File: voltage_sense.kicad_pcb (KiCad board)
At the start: 6 copper layers, 48 x 28 mm, 53 parts, among them IC1 DAC101C081CIMK_NOPB, J1 Conn_Coaxial, J2 Conn_01x04, J4 HDMI_A, J5 Conn_Coaxial, U1 OPA188xxDBV, U2 ADA4000-1, U3 OPA188xxDBV, U4 MCP4017T-103E_LT, U5 OPA1641, U6 24AA025UID, U9 LP2981A-33DBVT

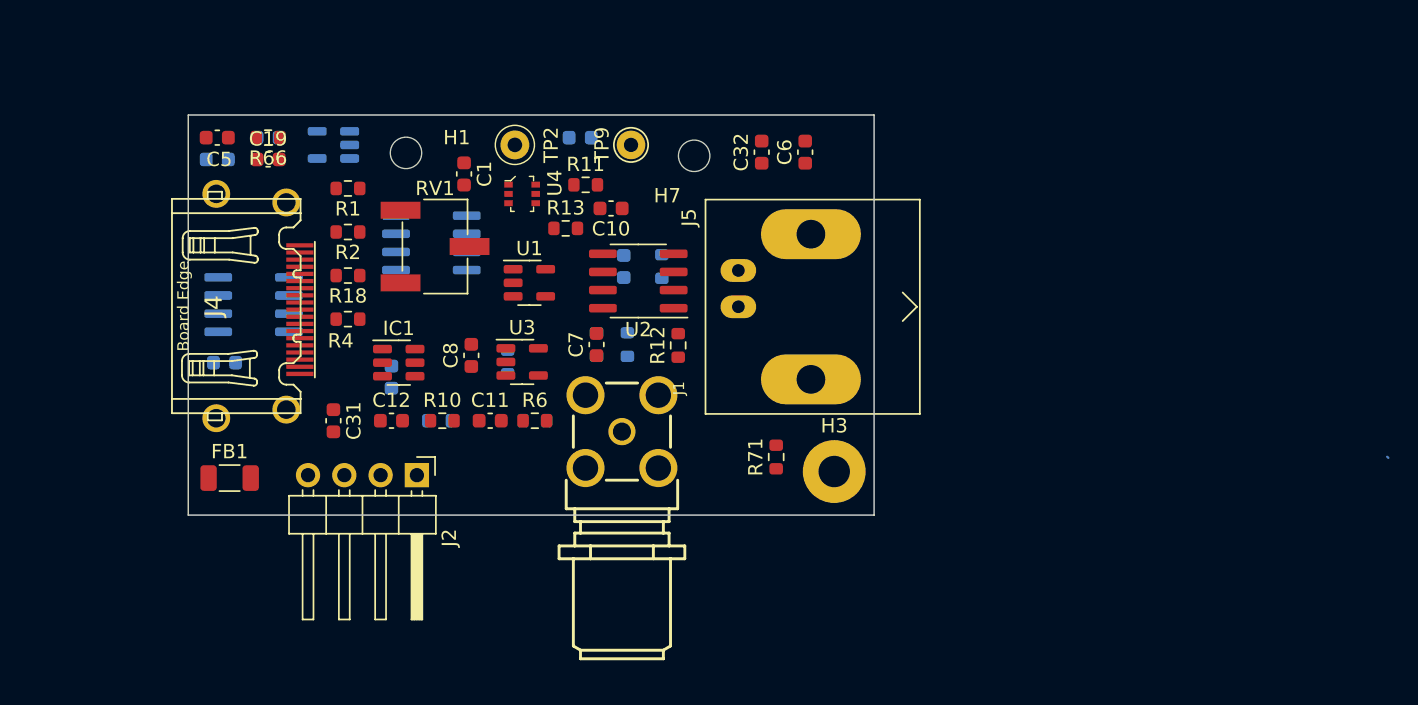
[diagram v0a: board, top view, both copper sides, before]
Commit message: found LCSC alternatives for some parts
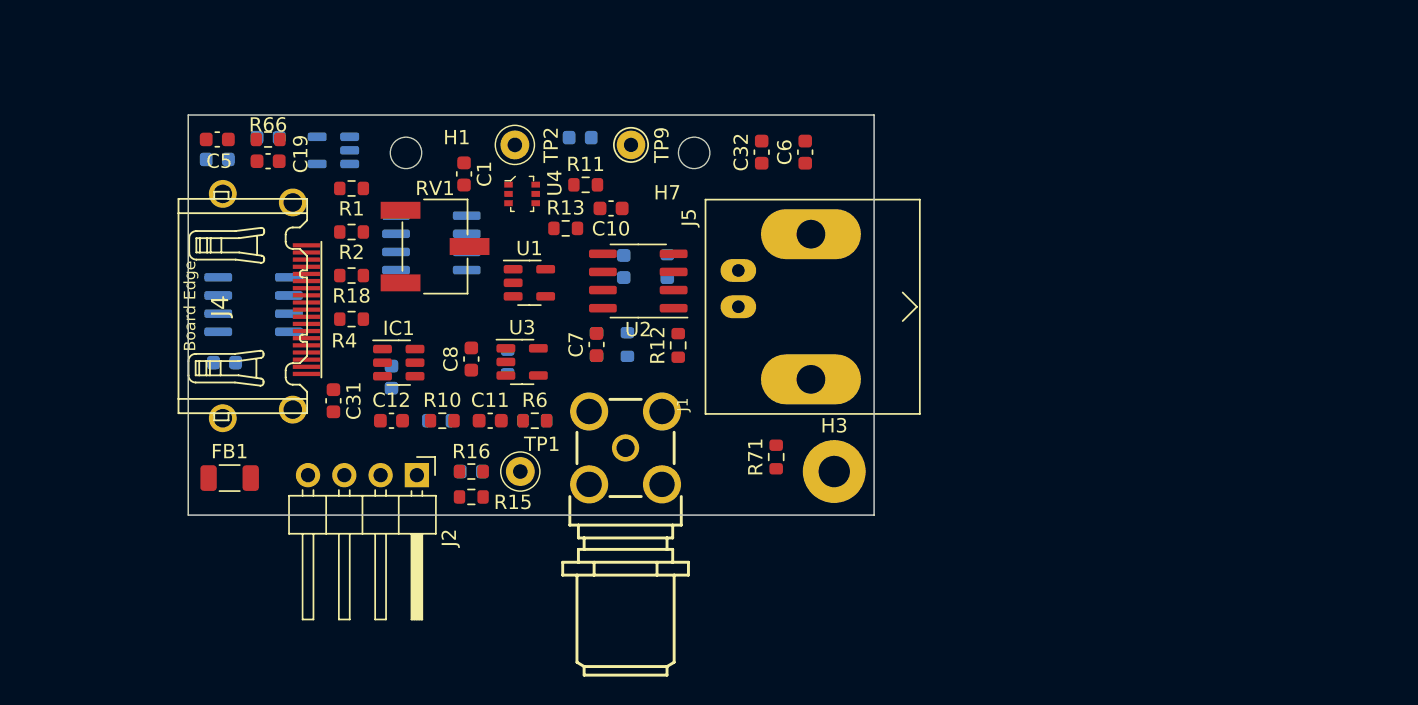
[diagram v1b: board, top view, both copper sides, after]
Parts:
- added C13: DNI, Capacitor_SMD:C_0603_1608Metric, B.Cu at (19.8, -3.05)
- added R15: 30k, Resistor_SMD:R_0603_1608Metric, F.Cu at (19.8, -1.27)
- added R16: 3k, Resistor_SMD:R_0603_1608Metric, F.Cu at (19.8, -3.05)
- added TP1: RCT-0C, digikey-footprints:Test_Point_D1.02mm, F.Cu at (23.2, -3.05)
- R14: value DNI -> 33
- moved C31 1.40 mm to (10.2, -8.00)
- moved J1 1.17 mm to (30.6, -4.70)
- moved J4 0.46 mm to (4.32, -14.6)
- moved R8 0.38 mm to (33.5, -17.4)
- moved U9 0.38 mm to (10.2, -25.5)
- moved C8 0.25 mm to (19.8, -10.9)
- moved R1 0.25 mm to (11.4, -22.9)
- moved R18 0.25 mm to (11.4, -16.8)
- moved R2 0.25 mm to (11.4, -19.8)
- moved R4 0.25 mm to (11.4, -13.7)
- moved H7 0.20 mm to (35.4, -25.4)
- moved C19 0.13 mm to (5.59, -24.8), turned to 180 degrees
- moved C5 0.13 mm to (2.03, -26.3)
- moved R66 0.13 mm to (5.59, -26.3)
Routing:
- net (no net): track 43.0 -> 0.00 mm
- net Net-(FB1-Pad1): track 40.6 -> 0.00 mm
- net /vsense/CMD: track 38.1 -> 0.00 mm
- net GND: track 34.4 -> 0.00 mm
- net /vsense/SMA_OUT: track 16.4 -> 0.00 mm
- net /vsense/AMP_OUT: track 15.4 -> 0.00 mm
- net +5V: track 14.3 -> 0.00 mm
- net /vsense/SDA: track 9.48 -> 0.00 mm
- net +3V3: track 4.87 -> 0.00 mm

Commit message: first draft of production files
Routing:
- net +3V3: track 0.00 -> 46.2 mm, vias 0 -> 3
- net GND: track 0.00 -> 39.3 mm, vias 0 -> 28
- net Net-(C12-Pad1): track 0.00 -> 31.9 mm, vias 0 -> 2
- net /vsense/SCL: track 0.00 -> 31.6 mm
- net Net-(C12-Pad2): track 0.00 -> 31.5 mm, vias 0 -> 1
- net Net-(FB1-Pad1): track 0.00 -> 29.5 mm
- net /vsense/SDA: track 0.00 -> 29.1 mm
- net Net-(C7-Pad2): track 0.00 -> 28.6 mm, vias 0 -> 2
- net Net-(R12-Pad1): track 0.00 -> 23.3 mm, vias 0 -> 1
- net /vsense/CC: track 0.00 -> 18.0 mm
- net Net-(C7-Pad1): track 0.00 -> 17.9 mm, vias 0 -> 1
- net Net-(C8-Pad2): track 0.00 -> 17.0 mm, vias 0 -> 1
- net /vsense/CMD: track 0.00 -> 15.4 mm
- net Net-(C1-Pad2): track 0.00 -> 14.9 mm
- net Net-(IC1-Pad1): track 0.00 -> 12.9 mm
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
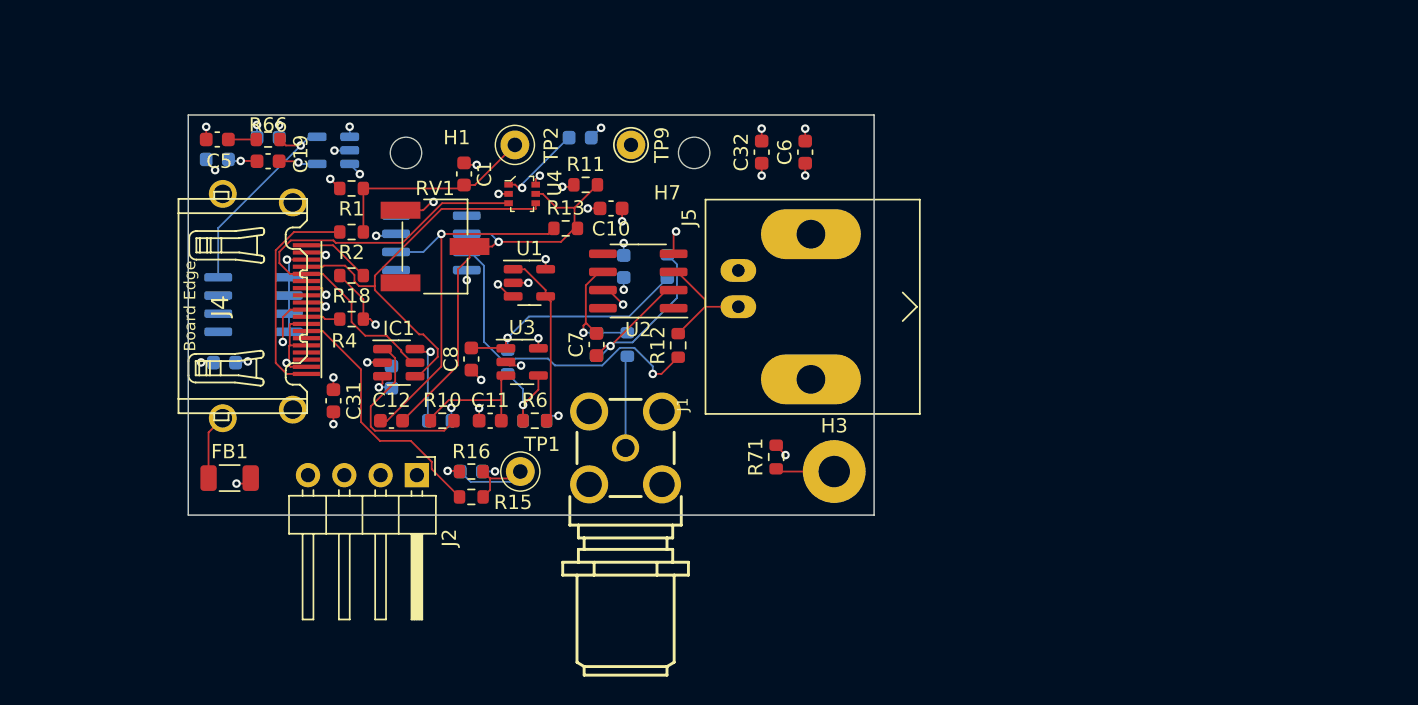
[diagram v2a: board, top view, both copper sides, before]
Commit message: moved SMA to same size as HDMI
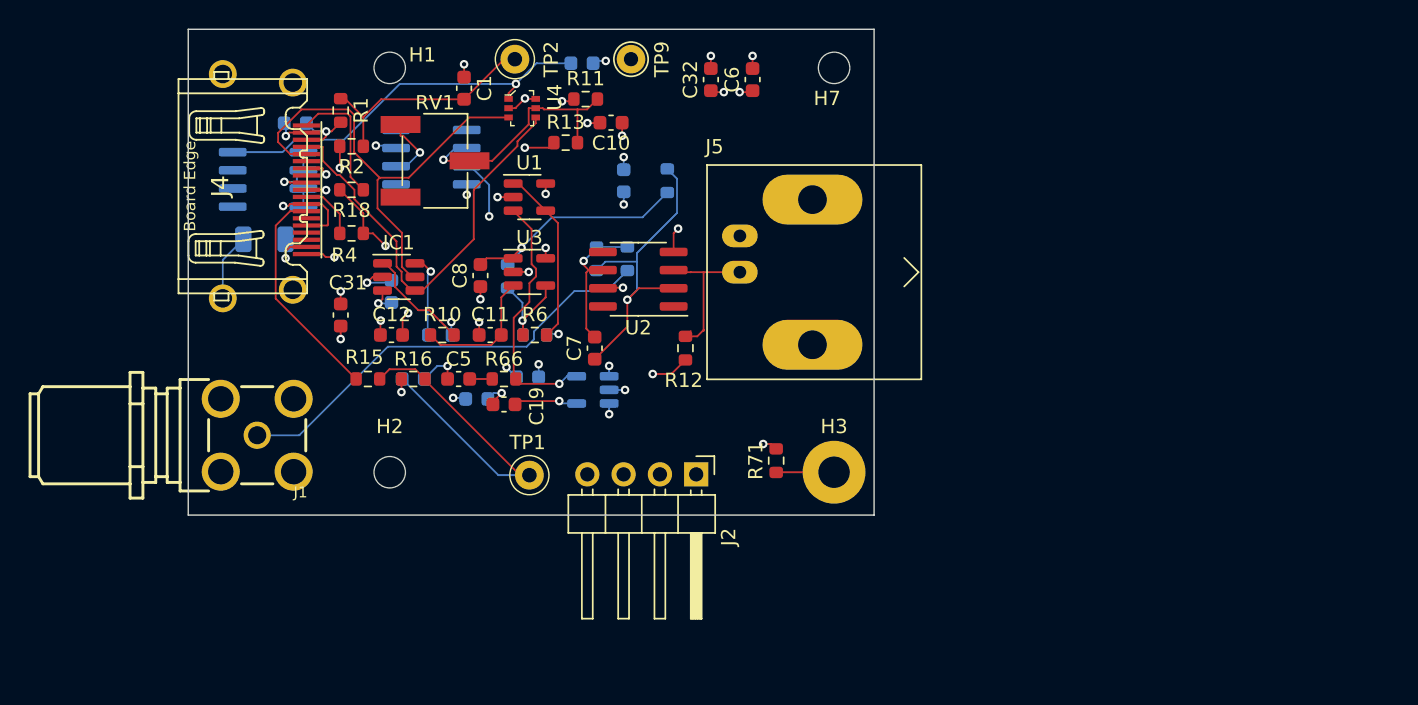
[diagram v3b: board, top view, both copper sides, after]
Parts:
- added H2: DNI, MountingHole:MountingHole_2.2mm_M2, F.Cu at (14.1, -3.00)
- C19: value 0.01u -> DNI
- FB1: moved to B.Cu
- moved J1 25.8 mm to (4.83, -5.59), turned to 180 degrees
- moved C2 24.7 mm to (20.2, -8.13)
- moved U9 24.7 mm to (28.3, -8.76)
- moved C4 24.7 mm to (23.7, -9.65)
- moved C5 23.8 mm to (18.9, -9.53)
- moved C19 23.7 mm to (22.1, -7.75)
- moved R66 23.5 mm to (22.1, -9.53)
- moved J2 19.5 mm to (35.5, -2.85)
- moved C39 17.5 mm to (7.49, -27.4), turned to 180 degrees
- moved FB1 16.9 mm to (5.33, -19.3)
- moved H7 11.5 mm to (45.2, -31.3)
- moved R15 11.0 mm to (12.6, -9.53)
- moved U6 8.82 mm to (5.59, -23.5)
- moved J4 8.39 mm to (4.32, -23.0)
- moved C13 7.65 mm to (15.7, -9.53)
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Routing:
- net /vsense/SMA_OUT: track 6.47 -> 31.0 mm
- net +3V3: track 46.2 -> 67.5 mm, vias 3 -> 2
- net Net-(C13-Pad2): track 9.30 -> 25.6 mm
- net GND: track 39.3 -> 44.7 mm, vias 28 -> 24
- net /vsense/CMD: track 15.4 -> 9.96 mm, vias 0 -> 2
- net Net-(IC1-Pad1): track 12.9 -> 7.65 mm
- net Net-(C7-Pad1): track 17.9 -> 22.6 mm
- net /vsense/AMP_OUT: track 4.86 -> 9.01 mm
- net Net-(C12-Pad1): track 31.9 -> 28.3 mm, vias 2 -> 3
- net +15V: track 11.0 -> 8.42 mm
- net /vsense/CC: track 18.0 -> 15.6 mm
- net Net-(J5-Pad1): track 8.49 -> 10.8 mm
- net /vsense/CAL_ADC: track 2.41 -> 4.19 mm
- net Net-(C19-Pad1): track 2.74 -> 4.48 mm
- net /vsense/SCL: track 31.6 -> 33.3 mm
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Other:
- board size 48 x 28 mm -> 48 x 34 mm

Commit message: files sent to JLCPCB; Order Y10-3276043A, SMT02305291257986-3276043A
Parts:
- C13, C2, C3, C39, C4, C47, C9, FB1, R14, R3, R5, R7, R8, R9, U9: moved to F.Cu
- moved C10 26.9 mm to (7.75, -11.8), turned to 90 degrees
- moved C12 23.7 mm to (37.5, -8.00), turned to 180 degrees
- moved R13 23.1 mm to (40.8, -8.00)
- moved R14 22.6 mm to (11.2, -6.60), turned to 0 degrees
- moved U5 22.3 mm to (31.4, -8.00)
- moved R11 16.4 mm to (44.1, -26.7), turned to 90 degrees
- moved U4 16.3 mm to (39.6, -26.8), turned to 0 degrees
- moved C2 11.0 mm to (26.3, -17.3), turned to 90 degrees
- moved RV1 10.6 mm to (27.8, -25.9)
- moved C31 9.19 mm to (19.3, -17.1), turned to 0 degrees
- moved C47 9.15 mm to (35.8, -27.7), turned to 0 degrees
- moved C4 8.69 mm to (32.1, -7.37), turned to 90 degrees
- moved FB1 7.81 mm to (4.32, -11.6)
- moved R2 6.38 mm to (11.4, -19.4)
- moved R10 6.16 mm to (12.4, -9.53), turned to 180 degrees
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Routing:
- net Net-(C7-Pad2): track 30.2 -> 60.2 mm
- net /vsense/SMA_OUT: track 31.0 -> 5.95 mm
- net Net-(R12-Pad1): track 23.5 -> 5.31 mm, vias 2 -> 1
- net Net-(C1-Pad2): track 16.4 -> 31.6 mm, vias 0 -> 1
- net /vsense/SDA: track 30.0 -> 45.1 mm, vias 0 -> 3
- net Net-(C12-Pad2): track 31.1 -> 44.0 mm, vias 2 -> 1
- net Net-(C12-Pad1): track 28.3 -> 40.6 mm, vias 3 -> 2
- net 3V3_BUF: track 12.4 -> 21.9 mm, vias 0 -> 2
- net /vsense/SCL: track 33.3 -> 41.5 mm, vias 0 -> 2
- net /vsense/CMD: track 9.96 -> 2.82 mm, vias 2 -> 0
- net Net-(C7-Pad1): track 22.6 -> 15.8 mm, vias 1 -> 0
- net Net-(R6-Pad1): track 7.89 -> 14.0 mm, vias 1 -> 2
- net Net-(C13-Pad2): track 25.6 -> 20.9 mm
- net /vsense/CC: track 15.6 -> 11.0 mm
- net /vsense/AMP_OUT: track 9.01 -> 4.60 mm
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
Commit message: Add files via upload
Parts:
- removed R7: 27.4k, Resistor_SMD:R_0603_1608Metric
- added C14: 0.1u, Capacitor_SMD:C_0603_1608Metric, F.Cu at (24.0, -23.4)
- added C15: 0.1u, Capacitor_SMD:C_0603_1608Metric, F.Cu at (17.3, -26.8)
- added C16: 0.1u, Capacitor_SMD:C_0603_1608Metric, B.Cu at (35.6, -19.6)
- added C17: 0.1u, Capacitor_SMD:C_0603_1608Metric, B.Cu at (34.5, -23.0)
- added C18: 0.1u, Capacitor_SMD:C_0603_1608Metric, B.Cu at (30.7, -5.21)
- added C20: 0.1u, Capacitor_SMD:C_0603_1608Metric, B.Cu at (34.9, -5.84)
- added C21: 10p, Capacitor_SMD:C_0603_1608Metric, F.Cu at (19.7, -15.9)
- added C22: 0.1u, Capacitor_SMD:C_0603_1608Metric, B.Cu at (18.8, -26.3)
- added C23: 1u, Capacitor_SMD:C_0603_1608Metric, B.Cu at (11.3, -25.3)
- added C24: 1u, Capacitor_SMD:C_0603_1608Metric, B.Cu at (17.0, -21.6)
- added R17: 100k, Resistor_SMD:R_0603_1608Metric, B.Cu at (20.6, -22.0)
- added R19: 100k, Resistor_SMD:R_0603_1608Metric, B.Cu at (20.6, -13.5)
- added R20: 100k, Resistor_SMD:R_0603_1608Metric, B.Cu at (20.6, -20.3)
- added R21: 100k, Resistor_SMD:R_0603_1608Metric, B.Cu at (20.6, -11.7)
- added R22: 100k, Resistor_SMD:R_0603_1608Metric, B.Cu at (20.6, -18.5)
- added R23: 100k, Resistor_SMD:R_0603_1608Metric, B.Cu at (20.6, -10.0)
- added R24: 100k, Resistor_SMD:R_0603_1608Metric, B.Cu at (20.6, -16.8)
- added R25: 100k, Resistor_SMD:R_0603_1608Metric, B.Cu at (20.6, -8.13)
- added R26: 3.01k, Resistor_SMD:R_0603_1608Metric, F.Cu at (28.3, -11.8)
- added R27: 10k, Resistor_SMD:R_0603_1608Metric, F.Cu at (13.8, -19.7)
- added R28: 10k, Resistor_SMD:R_0603_1608Metric, F.Cu at (15.6, -24.1)
- added R29: 4.99k, Resistor_SMD:R_0603_1608Metric, F.Cu at (24.5, -13.2)
- added R30: 3.01k, Resistor_SMD:R_0603_1608Metric, F.Cu at (31.9, -18.8)
- added R31: 49.9, Resistor_SMD:R_0603_1608Metric, F.Cu at (22.7, -19.8)
- added R32: DNI, Resistor_SMD:R_0603_1608Metric, B.Cu at (32.6, -15.7)
- added R33: 226k, Resistor_SMD:R_0603_1608Metric, B.Cu at (28.7, -25.8)
- added R34: 348k, Resistor_SMD:R_0603_1608Metric, B.Cu at (27.1, -17.9)
- added R35: 470k, Resistor_SMD:R_0603_1608Metric, B.Cu at (29.2, -15.6)
- added R36: 604k, Resistor_SMD:R_0603_1608Metric, B.Cu at (32.1, -25.8)
- added R38: DNI, Resistor_SMD:R_0603_1608Metric, B.Cu at (27.1, -8.89)
- added R39: 226k, Resistor_SMD:R_0603_1608Metric, B.Cu at (35.9, -13.7)
- added R40: 348k, Resistor_SMD:R_0603_1608Metric, B.Cu at (29.7, -13.7)
- added R41: 470k, Resistor_SMD:R_0603_1608Metric, B.Cu at (27.2, -11.3)
- added R42: 604k, Resistor_SMD:R_0603_1608Metric, B.Cu at (38.1, -10.2)
- added U10: TMUX6111PWR, covg-kicad:PW0016A_N, B.Cu at (32.6, -9.91)
- added U11: REF3440TIDBVR, covg-kicad:REF3440, B.Cu at (15.0, -25.4)
- added U7: ADA4000-2ARZ-R7, covg-kicad:R_8_ADI, F.Cu at (33.0, -13.2)
- added U8: TMUX6111PWR, covg-kicad:PW0016A_N, B.Cu at (30.7, -20.8)
- C11: value 0.1u -> 1u
- C31, C32: moved to B.Cu
- C7: value 4p -> 0.1u; moved to B.Cu
- C8: value 0.1u -> 1n
- J2: value Conn_01x04 -> DNI
- R10: value 27.4k -> 49.9k
- R12: value DNI -> 0
- R5: value 60.4k -> 100k; moved to B.Cu
- R6: value 33.2k -> 49.9k
- R8: value 3.01k -> DNI; moved to B.Cu
- R9: value 10k -> 4.99k
- RV1: footprint Potentiometer_SMD:Potentiometer_Bourns_3269W_Vertical -> covg-kicad:TRIM_3269W-1-103GLF
- U2: value ADA4000-1 -> TCA9555DBR; footprint Package_SO:SOIC-8_3.9x4.9mm_P1.27mm -> Package_SO:SSOP-24_5.3x8.2mm_P0.65mm; moved to B.Cu
- moved R8 30.1 mm to (4.83, -17.7), turned to 0 degrees
- moved R5 28.7 mm to (4.83, -19.7)
- moved C31 25.7 mm to (42.9, -27.2), turned to -90 degrees
- moved C6 22.7 mm to (35.7, -8.13), turned to 0 degrees
- moved C7 21.9 mm to (8.76, -21.3), turned to 0 degrees
- moved U5 21.4 mm to (38.2, -28.3)
- moved R13 19.2 mm to (33.8, -25.9), turned to 90 degrees
- moved U2 17.8 mm to (13.7, -16.0)
- moved C12 14.9 mm to (33.8, -22.5), turned to -90 degrees
- moved C10 14.7 mm to (20.2, -19.6)
- moved R6 13.8 mm to (16.4, -19.8), turned to 90 degrees
- moved TP9 11.5 mm to (20.2, -28.1)
- moved R15 7.18 mm to (15.6, -7.49), turned to 180 degrees
- moved R12 7.12 mm to (33.8, -18.8), turned to -90 degrees
- moved R16 6.72 mm to (22.2, -5.97)
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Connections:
- net 3V3_BUF renamed /vsense/2V_BUF
- C3 pad 2: +5V -> +4V
- C7 pad 1: Net-(C7-Pad1) -> GND
- C7 pad 2: Net-(C7-Pad2) -> +3V3
- IC1 pad 2: +5V -> +4V
- IC1 pad 4: /vsense/SDA -> SDA
- IC1 pad 5: /vsense/SCL -> SCL
- J4 pad 15: /vsense/SCL -> SCL
- J4 pad 16: /vsense/SDA -> SDA
- R11 pad 2: Net-(C12-Pad2) -> Net-(R11-Pad2)
- R12 pad 1: Net-(R12-Pad1) -> Net-(C12-Pad2)
- R13 pad 2: Net-(C12-Pad2) -> Net-(R11-Pad2)
- R14 pad 2: Net-(C7-Pad2) -> /vsense/gain_adjust_2/OUT
- R18 pad 1: /vsense/AMP_OUT -> /vsense/STG1_OUT
- R18 pad 2: Net-(C7-Pad2) -> /vsense/AMP_OUT
- R4 pad 1: /vsense/CAL_ADC -> /vsense/STG1_OUT
- R4 pad 2: Net-(C7-Pad2) -> /vsense/CAL_ADC
- R5 pad 1: Net-(C7-Pad1) -> +3V3
- R5 pad 2: Net-(C7-Pad2) -> Net-(R5-Pad2)
- R8 pad 1: Net-(C7-Pad1) -> Net-(R5-Pad2)
- R8 pad 2: Net-(C8-Pad2) -> GND
- R9 pad 1: Net-(C8-Pad2) -> /vsense/OFF_ADJ
- RV1 pad 2: Net-(C12-Pad2) -> Net-(R11-Pad2)
- U1 pad 3: +3V3 -> Net-(C24-Pad2)
- U2 pad 2: Net-(C7-Pad1) -> +3V3
- U2 pad 3: Net-(J5-Pad1) -> +3V3
- U2 pad 4: -15V -> /vsense/SW0
- U2 pad 5: unconnected-(U2-Pad5) -> /vsense/SW1
- U2 pad 6: Net-(C7-Pad2) -> /vsense/SW2
- U2 pad 7: +15V -> /vsense/SW3
- U2 pad 8: unconnected-(U2-Pad8) -> /vsense/SW4
- U3 pad 1: Net-(C8-Pad2) -> /vsense/OFF_ADJ
- U4 pad 3: /vsense/SCL -> SCL
- U4 pad 4: /vsense/SDA -> SDA
- U4 pad 5: Net-(C12-Pad2) -> Net-(R11-Pad2)
- U5 pad 2: Net-(C12-Pad2) -> Net-(R11-Pad2)
- U5 pad 3: Net-(R12-Pad1) -> Net-(C12-Pad2)
- U6 pad 5: /SDA -> SCL
- U6 pad 6: /SCL -> SDA
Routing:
- net GND: track 40.5 -> 105.0 mm, vias 27 -> 32
- net Net-(C7-Pad2): track 60.2 -> 0.00 mm, vias 2 -> 0
- net SDA: track 0.00 -> 59.2 mm, vias 0 -> 5
- net SCL: track 0.00 -> 57.7 mm, vias 0 -> 4
- net +5V: track 8.02 -> 57.9 mm, vias 6 -> 5
- net /vsense/STG1_OUT: track 0.00 -> 46.5 mm, vias 0 -> 3
- net /vsense/SDA: track 45.1 -> 0.00 mm, vias 3 -> 0
- net /vsense/SCL: track 41.5 -> 0.00 mm, vias 2 -> 0
- net /vsense/gain_adjust_2/OUT: track 0.00 -> 39.7 mm, vias 0 -> 2
- net +3V3: track 65.7 -> 30.8 mm, vias 2 -> 6
- net Net-(C12-Pad2): track 44.0 -> 13.1 mm
- net /vsense/SW7: track 0.00 -> 24.3 mm
- net /vsense/SW2: track 0.00 -> 22.0 mm
- net /vsense/SW3: track 0.00 -> 21.9 mm, vias 0 -> 2
- net Net-(R11-Pad2): track 0.00 -> 21.4 mm, vias 0 -> 1
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- added copper zone on In2.Cu, net +3V3
- removed copper zone on In2.Cu, net +5V
